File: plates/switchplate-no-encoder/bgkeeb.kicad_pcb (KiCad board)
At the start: 2 copper layers, 98.4 x 90.5 mm, 4 parts

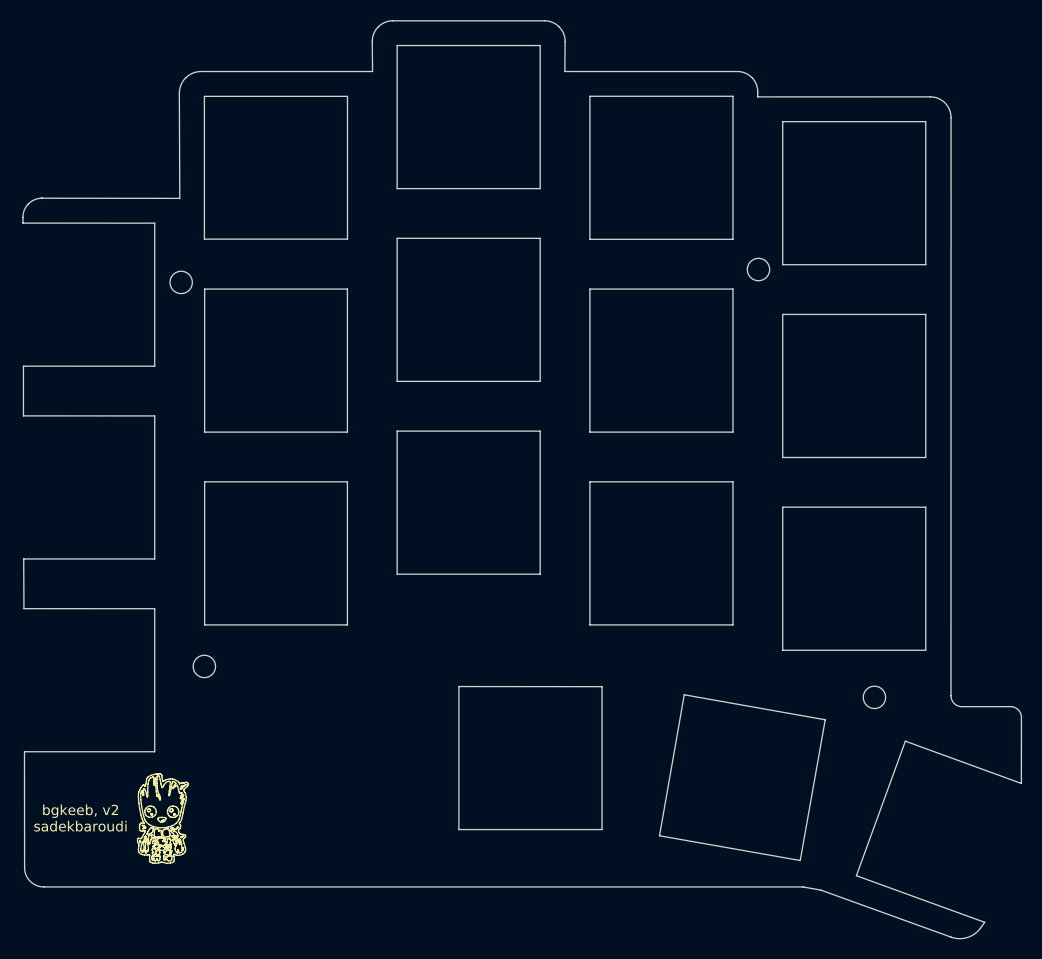
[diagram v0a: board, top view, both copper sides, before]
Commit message: outline issue fix
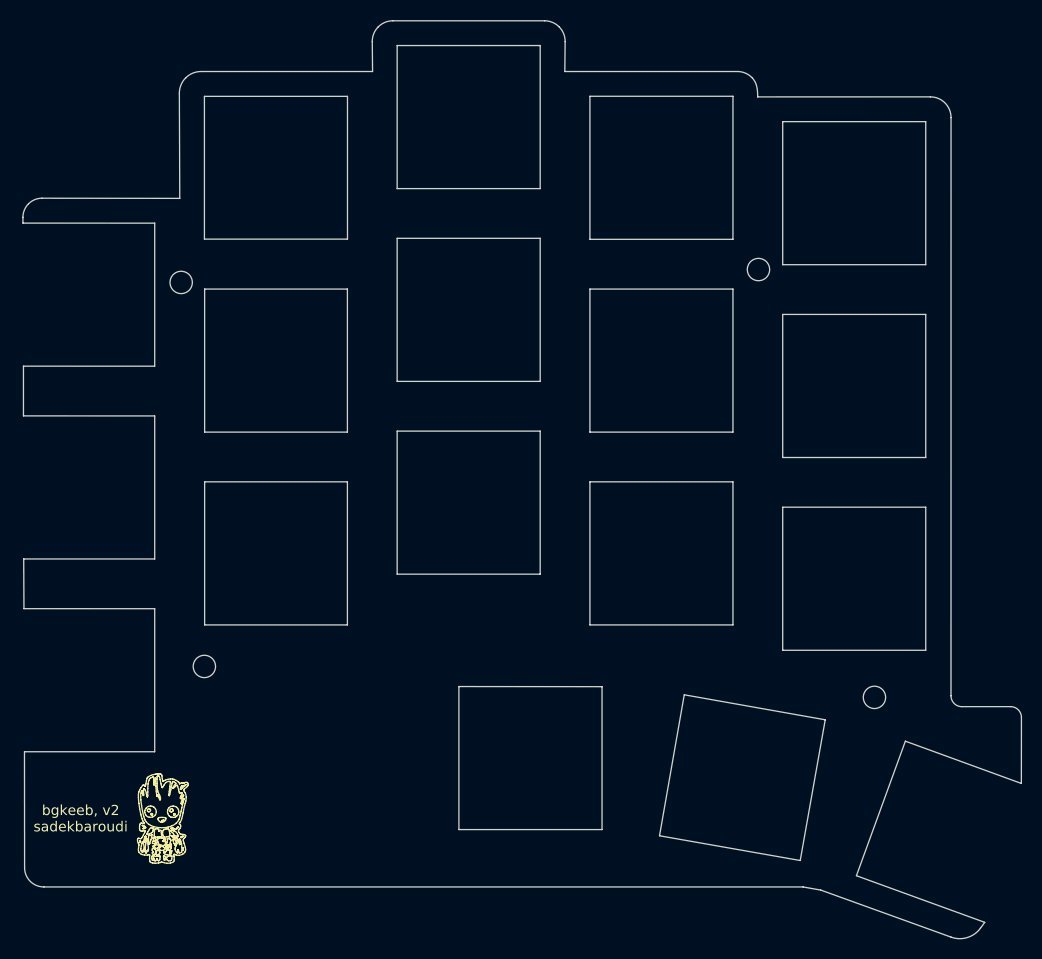
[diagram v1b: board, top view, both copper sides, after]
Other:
- outline, holes or cut-outs redrawn
- net class Default removed
- net class Power removed
